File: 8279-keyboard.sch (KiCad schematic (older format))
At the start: 27 parts

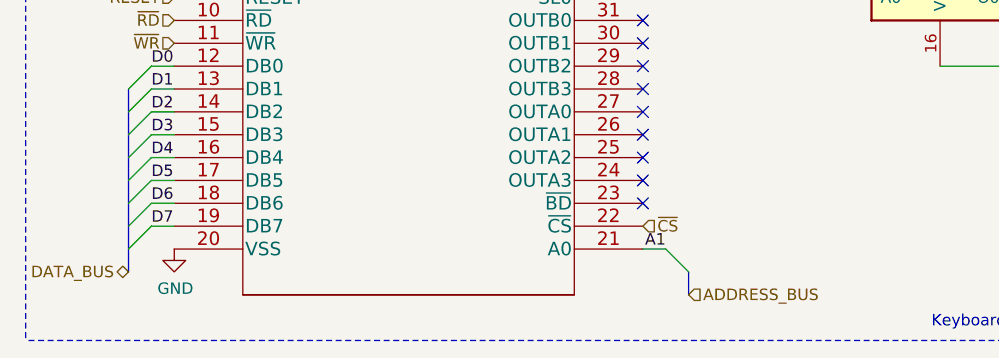
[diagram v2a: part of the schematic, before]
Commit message: Updates to pass ERC
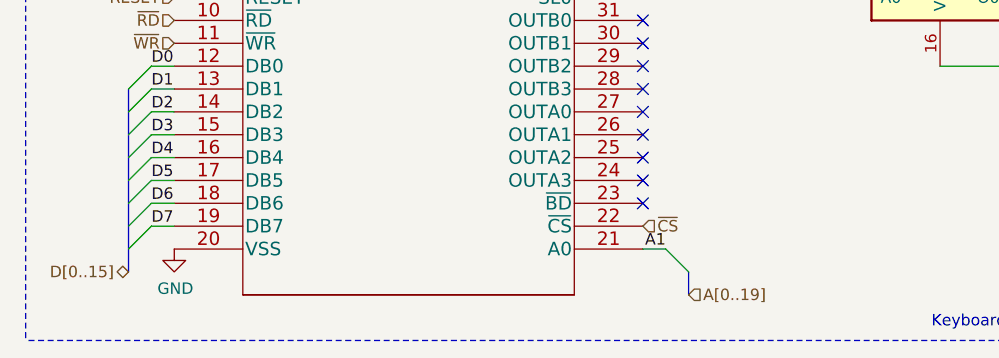
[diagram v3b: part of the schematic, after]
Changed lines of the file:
@@
 D7
 Text HLabel 1550 6850 0    50   BiDi ~ 0
-DATA_BUS
+D[0..15]
 Text Label 3900 6750 2    50   ~ 0
 A1
@@
 	4000 6850 4000 6950
 Text HLabel 4000 6950 2    50   Input ~ 0
-ADDRESS_BUS
+A[0..19]
 Text HLabel 1750 5750 0    50   Input ~ 0
 ~RD

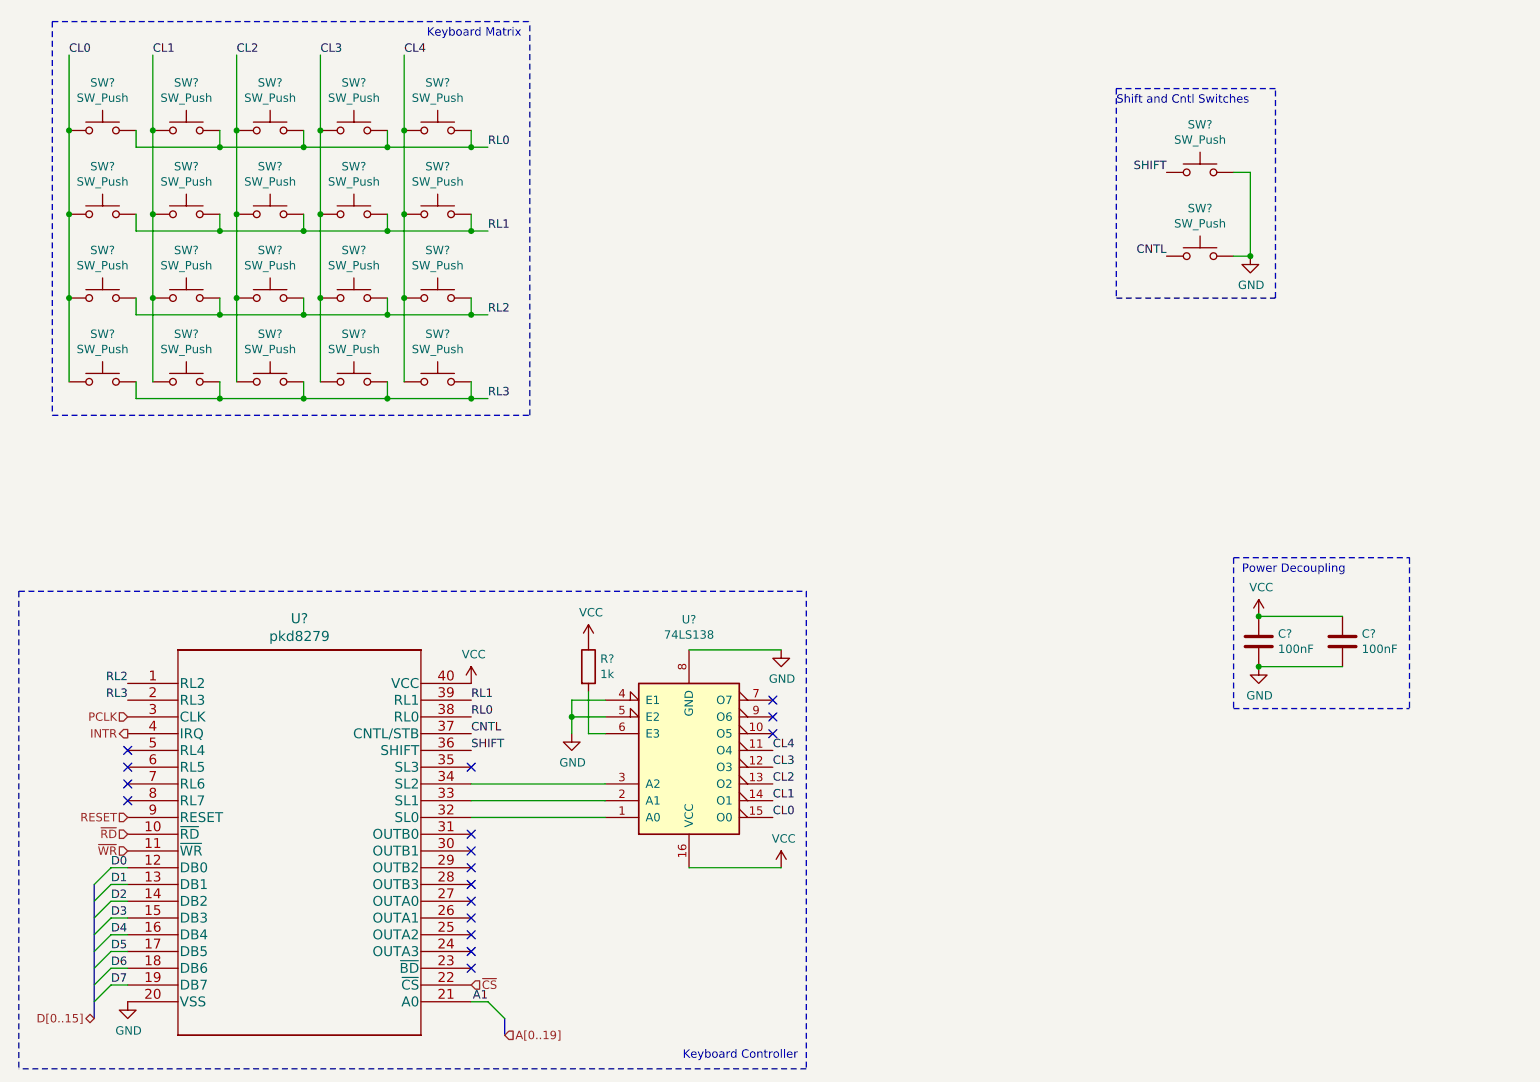
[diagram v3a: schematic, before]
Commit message: Assign footprints for most symbols
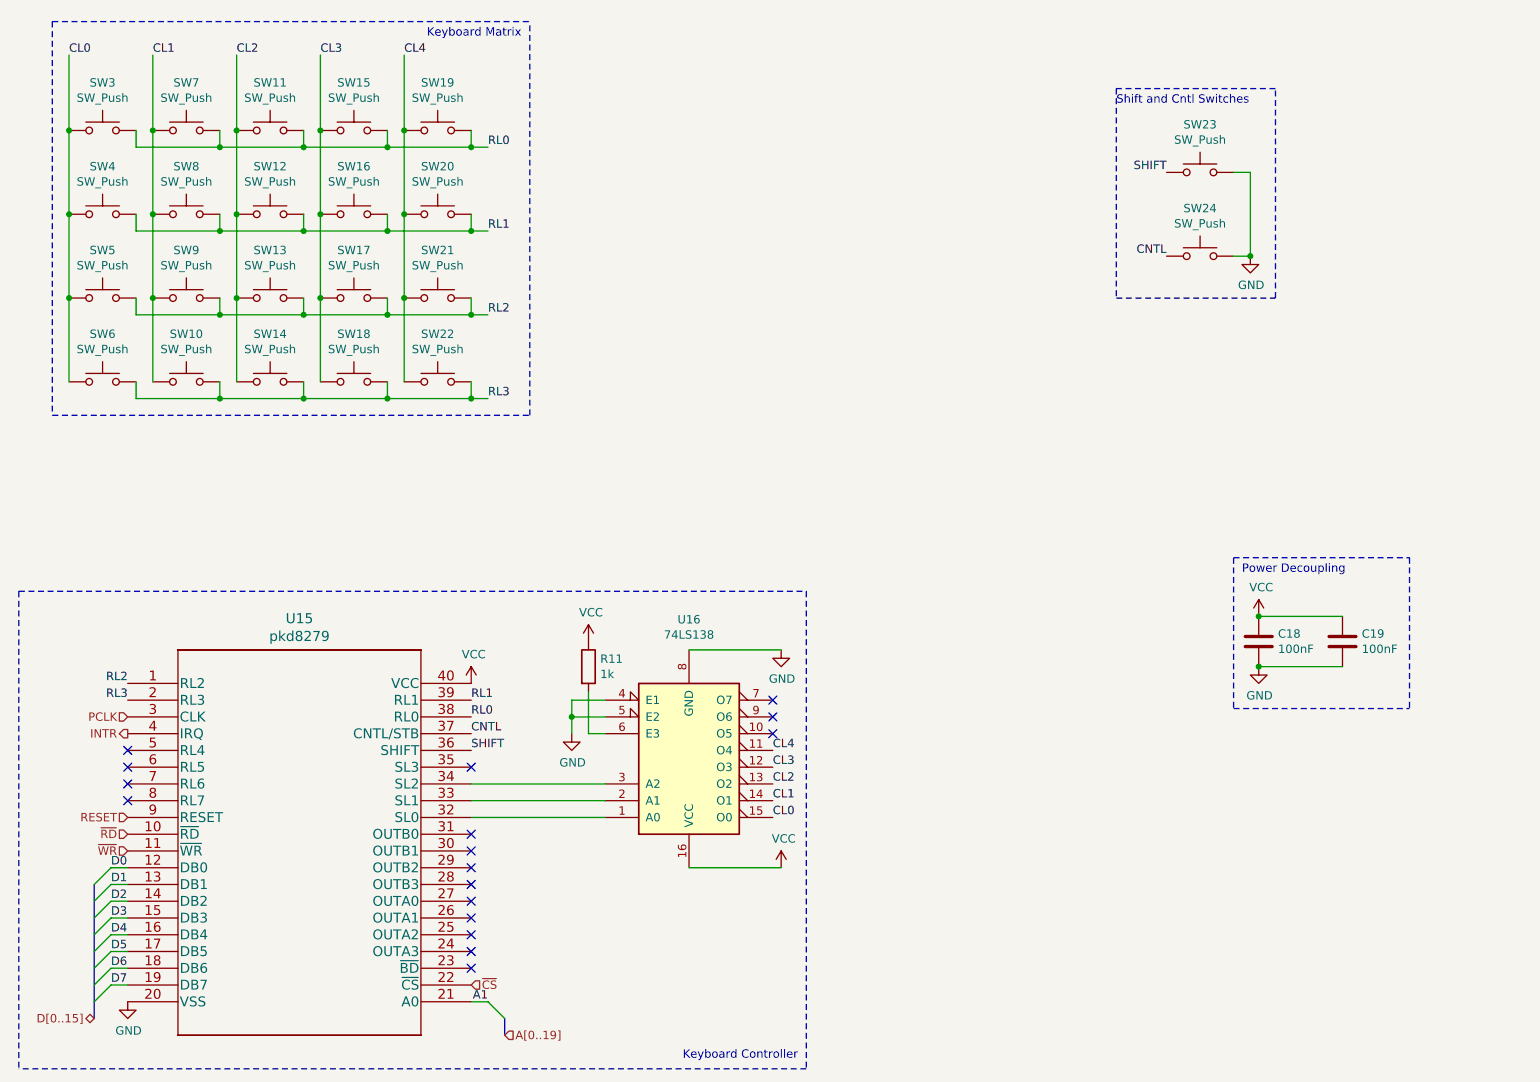
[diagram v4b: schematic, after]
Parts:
- C18, C19: renamed from C?; footprint (none) -> Capacitor_THT:C_Rect_L4.0mm_W2.5mm_P2.50mm
- R11: renamed from R?; footprint (none) -> Resistor_THT:R_Axial_DIN0207_L6.3mm_D2.5mm_P10.16mm_Horizontal
- SW10, SW11, SW12, SW13, SW14, SW15, SW16, SW17, SW18, SW19, SW20, SW21, SW22, SW23, SW24, SW3, SW4, SW5, SW6, SW7, SW8, SW9: renamed from SW?; footprint (none) -> Button_Switch_Keyboard:SW_Cherry_MX_1.00u_PCB
- U15: renamed from U?; footprint pkd8279 -> Libraries:pkd8279
- U16: renamed from U?; footprint (none) -> Package_DIP:DIP-16_W7.62mm

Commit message: assign footprints and edits
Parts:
- added D13, D14, D15, D16, D17, D18, D19, D20, D21, D22, D23, D24, D25, D26, D27, D28, D29, D30, D31, D32: D, Diode_THT:D_DO-35_SOD27_P7.62mm_Horizontal, symbol Device:D
- SW10: value SW_Push -> C1,R3
- SW11: value SW_Push -> C2,R0
- SW12: value SW_Push -> C2,R1
- SW13: value SW_Push -> C2,R2
- SW14: value SW_Push -> C2,R3
- SW15: value SW_Push -> C3,R0
- SW16: value SW_Push -> C3,R1
- SW17: value SW_Push -> C3,R2
- SW18: value SW_Push -> C3,R3
- SW19: value SW_Push -> C4,R0
- SW20: value SW_Push -> C4,R1
- SW21: value SW_Push -> C4,R2
- SW22: value SW_Push -> C4,R3
- SW3: value SW_Push -> C0,R0
- SW4: value SW_Push -> C0,R1
- SW5: value SW_Push -> C0,R2
- SW6: value SW_Push -> C0,R3
- SW7: value SW_Push -> C1,R0
- SW8: value SW_Push -> C1,R1
- SW9: value SW_Push -> C1,R2
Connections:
- net CL1: now also SW3.2, D13.1 (K)
- net RL0: now also D13.2 (A), D17.2 (A), D21.2 (A), D25.2 (A), D29.2 (A); no longer SW11.2, SW15.2, SW19.2, SW3.2, SW7.2
- net RL1: now also D14.2 (A), D18.2 (A), D22.2 (A), D26.2 (A), D30.2 (A); no longer SW12.2, SW16.2, SW20.2, SW4.2, SW8.2
- net RL2: now also D15.2 (A), D19.2 (A), D23.2 (A), D27.2 (A), D31.2 (A); no longer SW13.2, SW17.2, SW21.2, SW5.2, SW9.2
- net RL3: now also D16.2 (A), D20.2 (A), D24.2 (A), D28.2 (A), D32.2 (A); no longer SW10.2, SW14.2, SW18.2, SW22.2, SW6.2
- new net: D17.1 (K), SW7.2
- new net: D21.1 (K), SW11.2
- new net: D25.1 (K), SW15.2
- new net: D29.1 (K), SW19.2
- new net: D14.1 (K), SW4.2
- new net: D18.1 (K), SW8.2
- new net: D22.1 (K), SW12.2
- new net: D26.1 (K), SW16.2
- new net: D30.1 (K), SW20.2
- new net: D15.1 (K), SW5.2
- new net: D19.1 (K), SW9.2
- new net: D23.1 (K), SW13.2
- new net: D27.1 (K), SW17.2
- new net: D31.1 (K), SW21.2
- new net: D16.1 (K), SW6.2
- new net: D20.1 (K), SW10.2
- new net: D24.1 (K), SW14.2
- new net: D28.1 (K), SW18.2
- new net: D32.1 (K), SW22.2
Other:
- moved on the sheet: C18, C19, SW10, SW11, SW12, SW13, SW14, SW15, SW16, SW17, SW18, SW19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

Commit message: begin pcb layout
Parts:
- SW23: value SW_Push -> SHIFT
- SW24: value SW_Push -> CNTL
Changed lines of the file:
@@
 P 1750 1350
 F 0 "SW23" H 1750 1635 50  0000 C CNN
-F 1 "SW_Push" H 1750 1544 50  0000 C CNN
+F 1 "SHIFT" H 1750 1544 50  0000 C CNN
 F 2 "Button_Switch_Keyboard:SW_Cherry_MX_1.00u_PCB" H 1750 1550 50  0001 C CNN
 F 3 "~" H 1750 1550 50  0001 C CNN
@@
 P 1750 1850
 F 0 "SW24" H 1750 2135 50  0000 C CNN
-F 1 "SW_Push" H 1750 2044 50  0000 C CNN
+F 1 "CNTL" H 1750 2044 50  0000 C CNN
 F 2 "Button_Switch_Keyboard:SW_Cherry_MX_1.00u_PCB" H 1750 2050 50  0001 C CNN
 F 3 "~" H 1750 2050 50  0001 C CNN

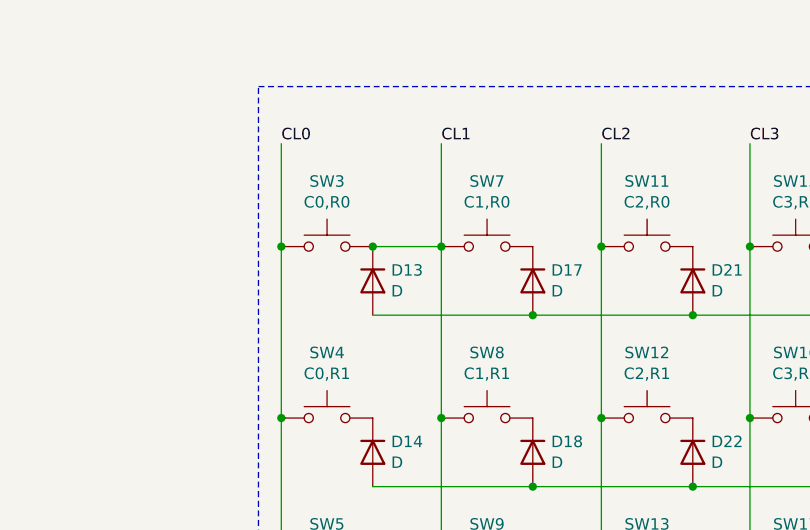
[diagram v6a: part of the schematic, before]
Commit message: more traces routed
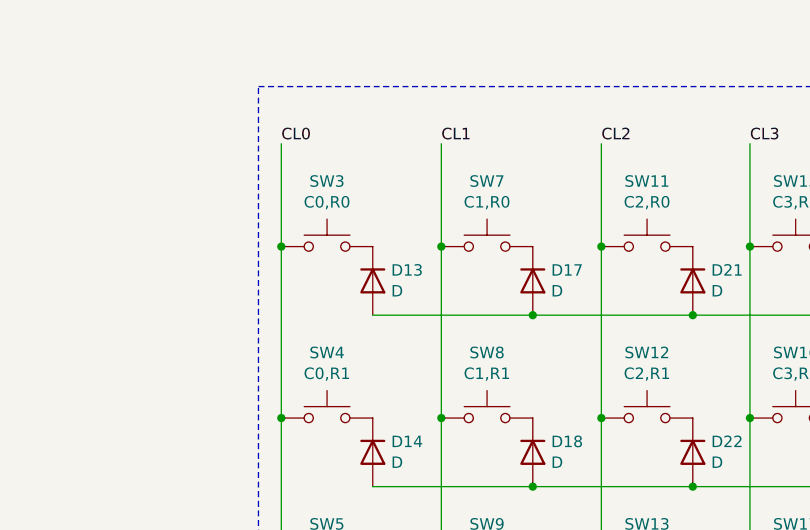
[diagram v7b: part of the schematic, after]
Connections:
- net CL1: no longer D13.1 (K), SW3.2
- new net: D13.1 (K), SW3.2
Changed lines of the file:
@@
 Wire Wire Line
 	7250 4100 7250 3350
-Wire Wire Line
-	7250 1850 6950 1850
 Connection ~ 7250 1850
 Connection ~ 7250 2600
@@
 Wire Wire Line
 	7250 3350 7250 2600
-Connection ~ 6950 1850
 Wire Wire Line
 	6550 1850 6550 2600
